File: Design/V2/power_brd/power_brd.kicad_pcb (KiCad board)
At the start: 2 copper layers, 54 parts, among them J1 XT60PW-M, J2 Conn_02x03_Odd_Even, J3 Conn_02x04_Odd_Even, J4 Conn_02x04_Odd_Even, U1 TPS5430DDAR, U2 TPS5430DDAR, U3 TPS5430DDAR, U4 TPS5430DDAR, U5 TPS5430DDAR

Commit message: laying out power board
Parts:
- moved U3 197.8 mm to (109.7, 79.5)
- moved L3 155.7 mm to (99.9, 82.5), turned to 180 degrees
- moved D3 151.5 mm to (104.5, 91.5), turned to -90 degrees
- moved C7 150.9 mm to (114.8, 77.0), turned to 90 degrees
- moved C9 135.7 mm to (109.7, 75.8)
- moved C11 135.3 mm to (98.5, 91.9), turned to -90 degrees
- moved C2 132.4 mm to (99.0, 58.4), turned to 90 degrees
- moved R2 130.1 mm to (102.5, 72.0)
- moved D6 129.1 mm to (98.5, 74.0), turned to 180 degrees
- moved D7 129.0 mm to (98.4, 76.1), turned to 180 degrees
- moved R6 128.9 mm to (102.2, 78.1)
- moved R1 126.7 mm to (98.5, 72.0)
- moved R5 125.6 mm to (98.4, 78.1)
- moved R11 124.3 mm to (102.5, 74.0), turned to 180 degrees
- moved R12 124.0 mm to (102.3, 76.1), turned to 180 degrees
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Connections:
- net Net-(D1-K) renamed /PH1
- net Net-(D2-K) renamed /PH3
- net Net-(D3-K) renamed /PH2
- net Net-(D4-K) renamed /PH4
- net Net-(D5-K) renamed /PH5
- C11 pad 1: VDD_SERVO_3 -> VDD_SERVO_3_4
- C2 pad 1: VDD_SERVO_1 -> VDD_SERVO_1_2
- D6 pad 2: VDD_SERVO_1 -> VDD_SERVO_1_2
- D7 pad 2: VDD_SERVO_3 -> VDD_SERVO_3_4
- J3 pad 1: VDD_SERVO_1 -> VDD_SERVO_3_4
- J3 pad 3: VDD_SERVO_1 -> VDD_SERVO_3_4
- J3 pad 5: VDD_SERVO_3 -> VDD_SERVO_1_2
- J3 pad 7: VDD_SERVO_3 -> VDD_SERVO_1_2
- L1 pad 2: VDD_SERVO_1 -> VDD_SERVO_1_2
- L3 pad 2: VDD_SERVO_3 -> VDD_SERVO_3_4
- R1 pad 1: VDD_SERVO_1 -> VDD_SERVO_1_2
- R5 pad 1: VDD_SERVO_3 -> VDD_SERVO_3_4
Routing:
- net VDD_SERVO_3_4: track 0.00 -> 33.4 mm
- net VDD_SERVO_1_2: track 0.00 -> 32.3 mm
- net /PH2: track 0.00 -> 22.5 mm
- net /PH1: track 0.00 -> 18.6 mm
- net Net-(U3-VSENSE): track 0.00 -> 12.7 mm, vias 0 -> 2
- net GND: track 0.00 -> 12.2 mm
- net Net-(U1-VSENSE): track 0.00 -> 8.03 mm
- net +BATT: track 0.00 -> 5.15 mm
- net Net-(U3-BOOT): track 0.00 -> 2.55 mm
- net Net-(U1-BOOT): track 0.00 -> 2.52 mm
- net Net-(D6-K): track 0.00 -> 1.95 mm
- net Net-(D7-K): track 0.00 -> 1.87 mm
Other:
- copper layers 2 -> 4

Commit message: mostly finished power board layout
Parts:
- moved U4 213.0 mm to (124.8, 79.5)
- moved U2 213.0 mm to (124.8, 68.0)
- moved U5 206.4 mm to (118.2, 91.4), turned to 90 degrees
- moved L2 190.9 mm to (135.9, 67.4)
- moved L4 190.8 mm to (135.8, 82.2)
- moved D4 176.5 mm to (131.0, 91.3), turned to -90 degrees
- moved D2 175.3 mm to (131.0, 58.0), turned to 90 degrees
- moved L5 174.1 mm to (117.8, 102.8)
- moved C12 172.7 mm to (137.9, 91.2), turned to -90 degrees
- moved C6 171.0 mm to (137.9, 57.9), turned to 90 degrees
- moved D9 168.8 mm to (138.0, 75.8)
- moved D8 168.7 mm to (137.9, 73.7)
- moved R3 164.6 mm to (137.9, 71.7), turned to 180 degrees
- moved C15 164.5 mm to (128.7, 102.5)
- moved R7 161.9 mm to (138.0, 77.7), turned to 180 degrees
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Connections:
- net VDD_SERVO_5 renamed VDD_SERVO_5_6
- net VDD_SERVO_7 renamed VDD_SERVO_7_8
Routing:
- net +BATT: track 5.15 -> 83.0 mm
- net VDD_FC: track 0.00 -> 41.4 mm
- net VDD_SERVO_5_6: track 0.00 -> 35.1 mm
- net VDD_SERVO_7_8: track 0.00 -> 32.3 mm
- net GND: track 12.2 -> 41.4 mm, vias 0 -> 152
- net /PH5: track 0.00 -> 27.7 mm
- net Net-(U4-VSENSE): track 0.00 -> 24.8 mm, vias 0 -> 2
- net Net-(U2-VSENSE): track 0.00 -> 22.8 mm, vias 0 -> 2
- net /PH4: track 0.00 -> 17.3 mm
- net /PH3: track 0.00 -> 15.5 mm
- net Net-(U5-VSENSE): track 0.00 -> 4.02 mm
- net Net-(U5-BOOT): track 0.00 -> 2.62 mm
- net Net-(U2-BOOT): track 0.00 -> 2.49 mm
- net Net-(U4-BOOT): track 0.00 -> 2.45 mm
- net Net-(D8-K): track 0.00 -> 1.83 mm
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- added copper zone on B.Cu, net GND
- added copper zone on F.Cu, net GND
- added copper zone on In1.Cu, net GND
- added copper zone on In2.Cu, net GND
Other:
- board outline added: 70 x 75 mm

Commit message: power board
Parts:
- added H1: MountingHole_Pad, MountingHole:MountingHole_3.2mm_M3_Pad_Via, F.Cu at (90.8, 48.4)
- added H2: MountingHole_Pad, MountingHole:MountingHole_3.2mm_M3_Pad_Via, F.Cu at (91.6, 112.2)
- added H3: MountingHole_Pad, MountingHole:MountingHole_3.2mm_M3_Pad_Via, F.Cu at (144.3, 111.9)
- added H4: MountingHole_Pad, MountingHole:MountingHole_3.2mm_M3_Pad_Via, F.Cu at (147.5, 48.7)
- J4: moved to B.Cu
- moved J4 8.72 mm to (142.2, 78.6)
- moved J3 3.44 mm to (94.0, 78.6)
- moved J2 1.36 mm to (120.3, 108.1)
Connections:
- J4 pad 1: VDD_SERVO_5_6 -> VDD_SERVO_7_8
- J4 pad 3: VDD_SERVO_5_6 -> VDD_SERVO_7_8
- J4 pad 5: VDD_SERVO_7_8 -> VDD_SERVO_5_6
- J4 pad 7: VDD_SERVO_7_8 -> VDD_SERVO_5_6
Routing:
- net VDD_FC: track 41.4 -> 24.2 mm
- net VDD_SERVO_5_6: track 35.1 -> 20.8 mm
- net VDD_SERVO_3_4: track 33.4 -> 21.3 mm
- net VDD_SERVO_7_8: track 32.3 -> 20.4 mm
- net VDD_SERVO_1_2: track 32.3 -> 20.7 mm
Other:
- board size 70 x 75 mm -> 73.5 x 80.5 mm

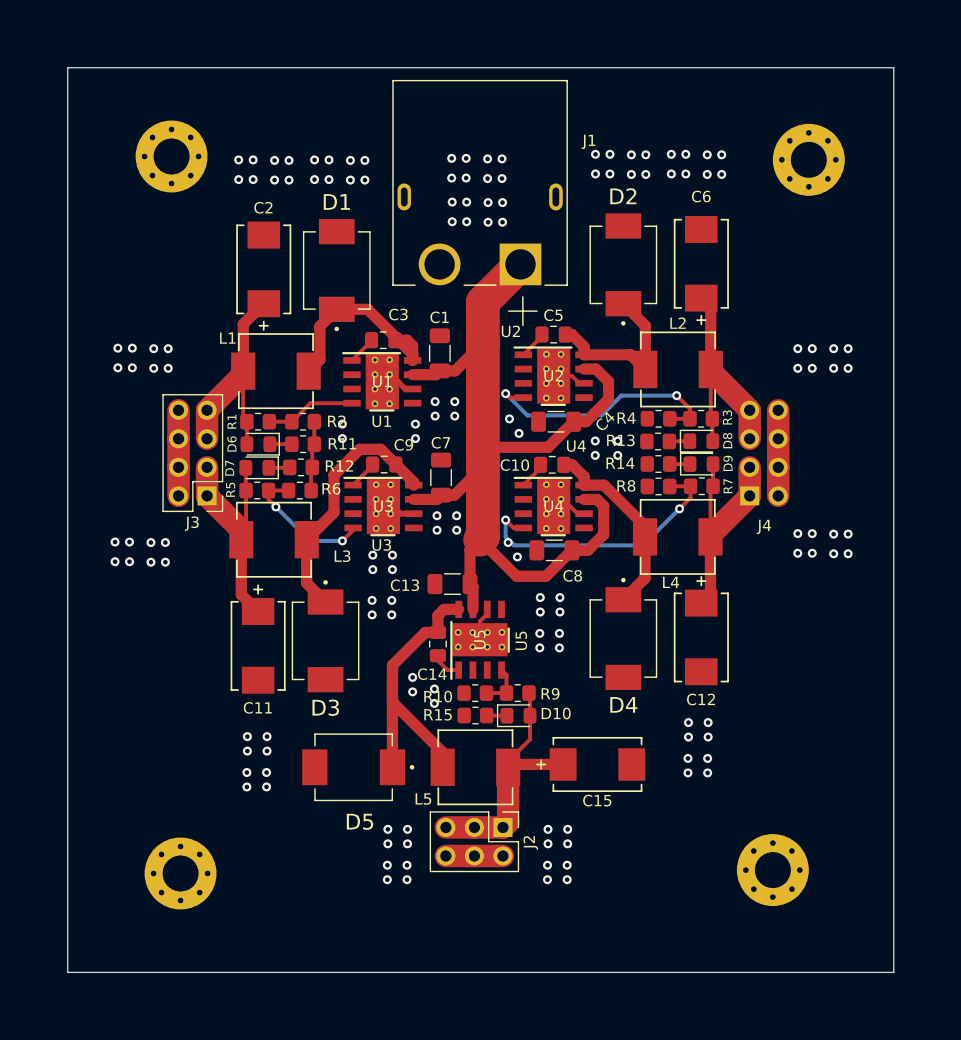
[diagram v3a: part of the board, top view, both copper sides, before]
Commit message: fc and power board sent out for assembly
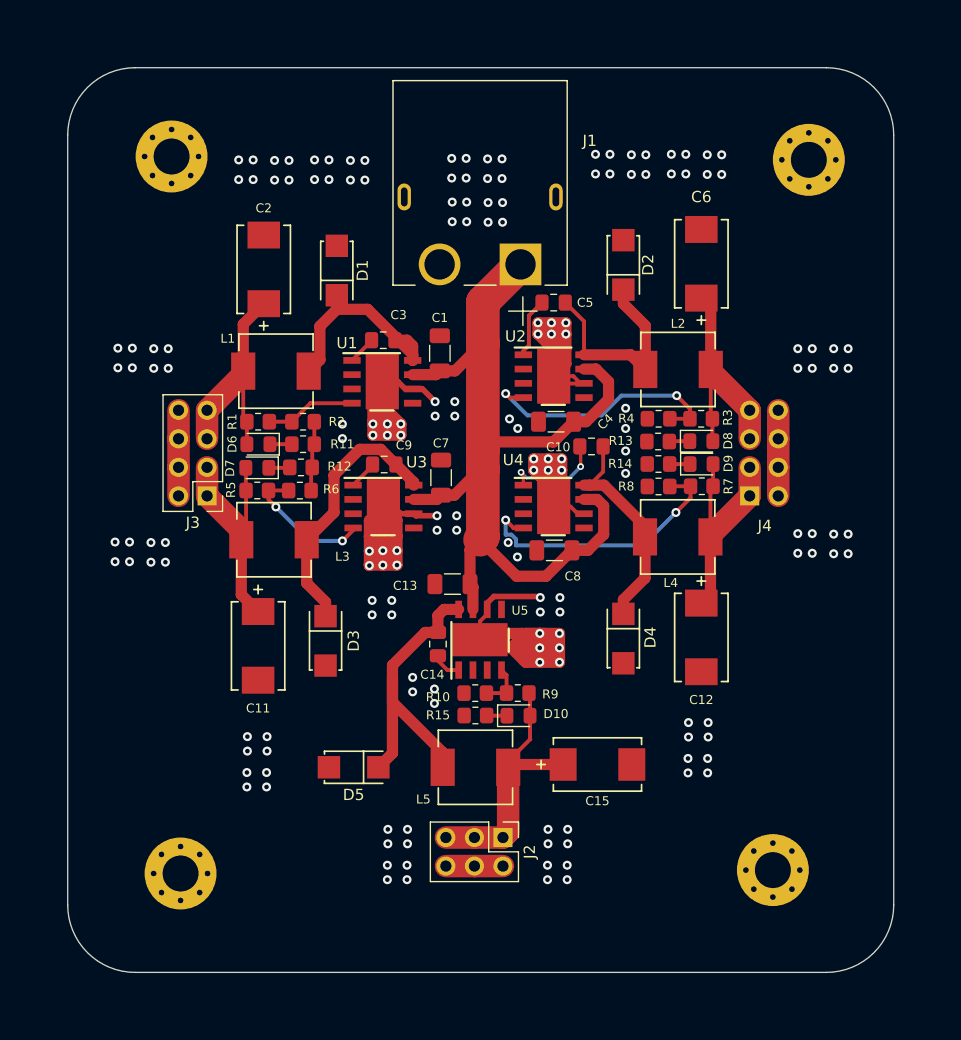
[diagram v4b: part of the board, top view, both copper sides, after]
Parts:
- D1, D2, D3, D4, D5: footprint Diodes:SS34_DO214AB -> Diodes:SMA_L4.3-W2.6-LS5.2-RD
- moved C10 3.85 mm to (128.2, 74.2)
- moved C5 2.85 mm to (124.8, 61.4)
- moved J2 0.90 mm to (120.3, 109.0)
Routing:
- net GND: track 41.4 -> 178.0 mm, vias 152 -> 172
- net Net-(U4-BOOT): track 2.45 -> 8.97 mm, vias 0 -> 2
- net /PH3: track 15.5 -> 19.2 mm
- net Net-(U2-BOOT): track 2.49 -> 5.33 mm
- net /PH4: track 17.3 -> 19.5 mm
- net /PH1: track 18.6 -> 19.8 mm
- net /PH2: track 22.5 -> 23.8 mm
- net VDD_FC: track 24.2 -> 25.1 mm
- net /PH5: track 27.7 -> 28.2 mm
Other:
- outline, holes or cut-outs redrawn
